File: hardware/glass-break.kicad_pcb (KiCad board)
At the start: 2 copper layers, 83.5 x 48.5 mm, 25 parts, among them P1 USB_OTG, U11 SPX3819

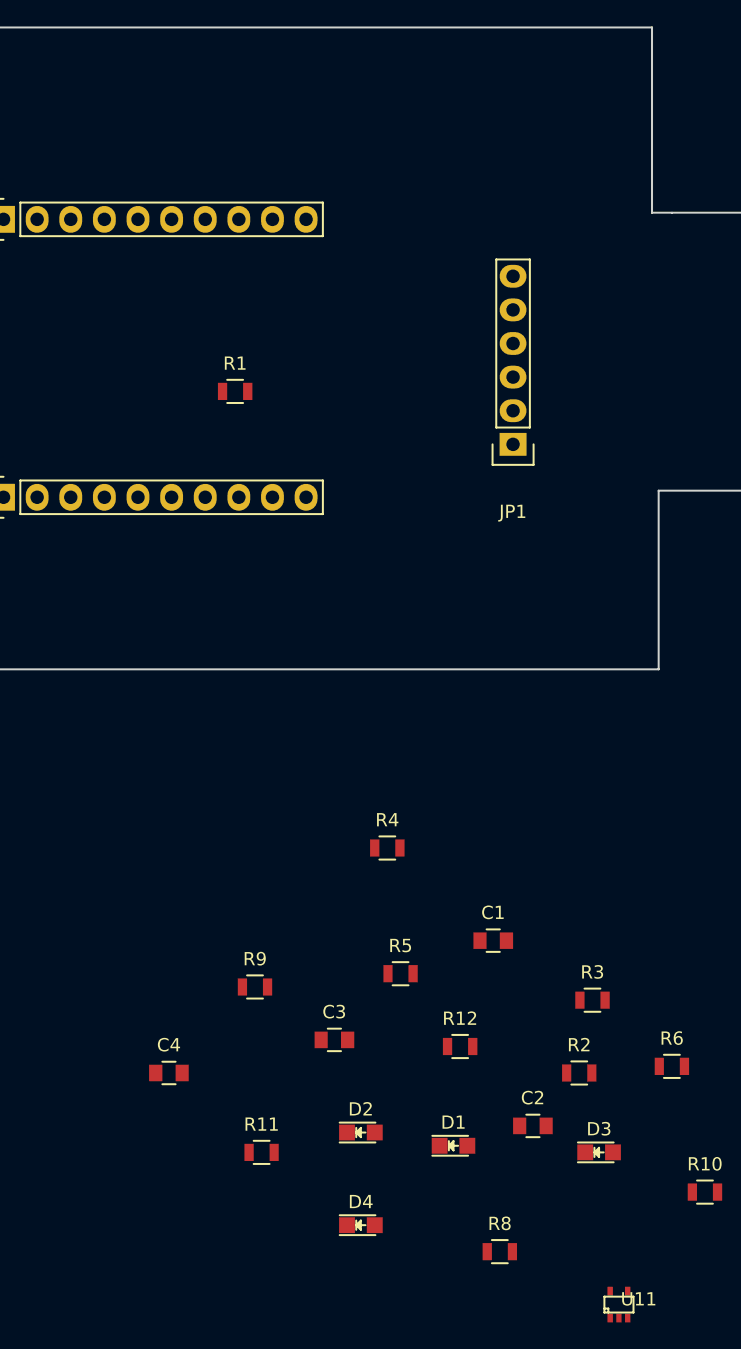
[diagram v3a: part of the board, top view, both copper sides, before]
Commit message: added dimensions update
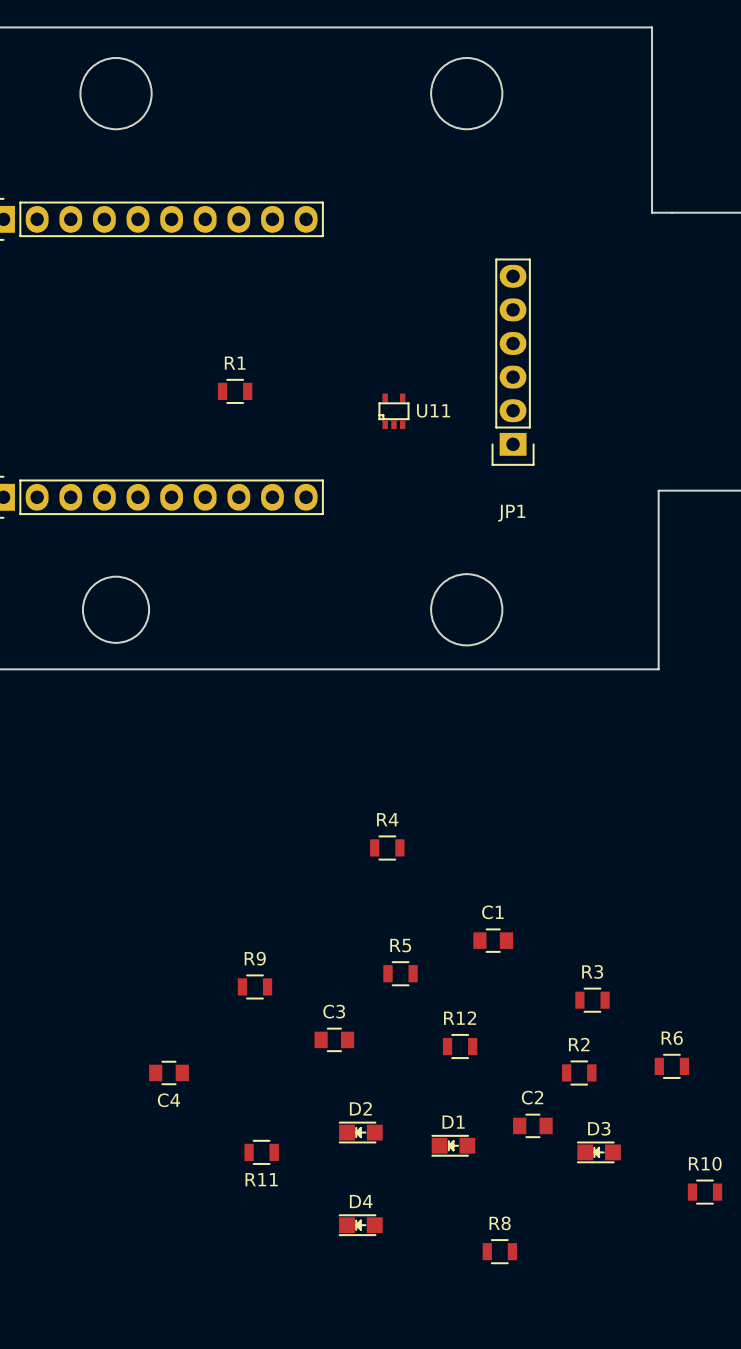
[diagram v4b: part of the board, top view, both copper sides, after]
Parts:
- moved U11 69.6 mm to (170.5, 74.0)
- turned C4 to 180 degrees
- turned R11 to 180 degrees
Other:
- outline, holes or cut-outs redrawn
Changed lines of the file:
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@@
     (area 120.924999 44.924999 204.575001 93.575001)
     (thickness 1.6)
-    (drawings 31)
+    (drawings 35)
     (tracks 0)
     (zones 0)
@@
   )
   (module Capacitors_SMD:C_0805 (layer F.Cu)
-    (at 153.5 124)
+    (at 153.5 124 180)
     (descr "Capacitor SMD 0805, reflow soldering, AVX (see smccp.pdf)")
     (tags "capacitor 0805")
     (attr smd)
-    (fp_text reference C4 (at 0 -2.1) (layer F.SilkS)
-      (effects (font (size 1 1) (thickness 0.15)))
-    )
-    (fp_text value "4.7 uF" (at 0 2.1) (layer F.Fab)
+    (fp_text reference C4 (at 0 -2.1 180) (layer F.SilkS)
+      (effects (font (size 1 1) (thickness 0.15)))
+    )
+    (fp_text value "4.7 uF" (at 0 2.1 180) (layer F.Fab)
       (effects (font (size 1 1) (thickness 0.15)))
     )
@@
     (fp_line (start 0.5 -0.85) (end -0.5 -0.85) (layer F.SilkS) (width 0.15))
     (fp_line (start -0.5 0.85) (end 0.5 0.85) (layer F.SilkS) (width 0.15))
-    (pad 1 smd rect (at -1 0) (size 1 1.25) (layers F.Cu F.Paste F.Mask)
+    (pad 1 smd rect (at -1 0 180) (size 1 1.25) (layers F.Cu F.Paste F.Mask)
       (net 6 "Net-(C4-Pad1)"))
-    (pad 2 smd rect (at 1 0) (size 1 1.25) (layers F.Cu F.Paste F.Mask)
+    (pad 2 smd rect (at 1 0 180) (size 1 1.25) (layers F.Cu F.Paste F.Mask)
       (net 7 "Net-(C4-Pad2)"))
     (model Capacitors_SMD.3dshapes/C_0805.wrl
@@
   )
   (module Resistors_SMD:R_0805 (layer F.Cu)
-    (at 160.5 130)
-    (descr "Resistor SMD 0805, reflow soldering, Vishay (see dcrcw.pdf)")
-    (tags "resistor 0805")
-    (attr smd)
-    (fp_text reference R11 (at 0 -2.1) (layer F.SilkS)
-      (effects (font (size 1 1) (thickness 0.15)))
-    )
-    (fp_text value 2.2K (at 0 2.1) (layer F.Fab)
-      (effects (font (size 1 1) (thickness 0.15)))
-    )
-    (fp_line (start -1.6 -1) (end 1.6 -1) (layer F.CrtYd) (width 0.05))
-    (fp_line (start -1.6 1) (end 1.6 1) (layer F.CrtYd) (width 0.05))
-    (fp_line (start -1.6 -1) (end -1.6 1) (layer F.CrtYd) (width 0.05))
-    (fp_line (start 1.6 -1) (end 1.6 1) (layer F.CrtYd) (width 0.05))
-    (fp_line (start 0.6 0.875) (end -0.6 0.875) (layer F.SilkS) (width 0.15))
-    (fp_line (start -0.6 -0.875) (end 0.6 -0.875) (layer F.SilkS) (width 0.15))
-    (pad 1 smd rect (at -0.95 0) (size 0.7 1.3) (layers F.Cu F.Paste F.Mask)
+    (at 160.5 130 180)
+    (descr "Resistor SMD 0805, reflow soldering, Vishay (see dcrcw.pdf)")
+    (tags "resistor 0805")
+    (attr smd)
+    (fp_text reference R11 (at 0 -2.1 180) (layer F.SilkS)
+      (effects (font (size 1 1) (thickness 0.15)))
+    )
+    (fp_text value 2.2K (at 0 2.1 180) (layer F.Fab)
+      (effects (font (size 1 1) (thickness 0.15)))
+    )
+    (fp_line (start -1.6 -1) (end 1.6 -1) (layer F.CrtYd) (width 0.05))
+    (fp_line (start -1.6 1) (end 1.6 1) (layer F.CrtYd) (width 0.05))
+    (fp_line (start -1.6 -1) (end -1.6 1) (layer F.CrtYd) (width 0.05))
+    (fp_line (start 1.6 -1) (end 1.6 1) (layer F.CrtYd) (width 0.05))
+    (fp_line (start 0.6 0.875) (end -0.6 0.875) (layer F.SilkS) (width 0.15))
+    (fp_line (start -0.6 -0.875) (end 0.6 -0.875) (layer F.SilkS) (width 0.15))
+    (pad 1 smd rect (at -0.95 0 180) (size 0.7 1.3) (layers F.Cu F.Paste F.Mask)
       (net 11 +3V3))
-    (pad 2 smd rect (at 0.95 0) (size 0.7 1.3) (layers F.Cu F.Paste F.Mask)
+    (pad 2 smd rect (at 0.95 0 180) (size 0.7 1.3) (layers F.Cu F.Paste F.Mask)
       (net 7 "Net-(C4-Pad2)"))
     (model Resistors_SMD.3dshapes/R_0805.wrl
@@
   )
   (module TO_SOT_Packages_SMD:SC-70-5 (layer F.Cu)
-    (at 187.5 141.5)
+    (at 170.5 74)
     (descr "SC70-5 SOT323-5")
     (attr smd)
-    (fp_text reference U11 (at 1.5 -0.4) (layer F.SilkS)
-      (effects (font (size 1 1) (thickness 0.15)))
-    )
-    (fp_text value SPX3819 (at 2.2 0.3) (layer F.Fab)
+    (fp_text reference U11 (at 3 0) (layer F.SilkS)
+      (effects (font (size 1 1) (thickness 0.15)))
+    )
+    (fp_text value SPX3819 (at 0.5 2) (layer F.Fab)
       (effects (font (size 1 1) (thickness 0.15)))
     )
@@
     )
   )
+  (gr_circle (center 176 89) (end 178.5 88) (layer Edge.Cuts) (width 0.15))
+  (gr_circle (center 176 50) (end 178.5 49) (layer Edge.Cuts) (width 0.15))
+  (gr_circle (center 149.5 50) (end 152 49) (layer Edge.Cuts) (width 0.15))
+  (gr_circle (center 149.5 89) (end 151.5 87.5) (layer Edge.Cuts) (width 0.15))
   (gr_line (start 190 59) (end 191.5 59) (angle 90) (layer Edge.Cuts) (width 0.15))
   (gr_line (start 190 45) (end 190 59) (angle 90) (layer Edge.Cuts) (width 0.15))
